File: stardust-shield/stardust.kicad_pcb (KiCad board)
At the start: 2 copper layers, 154.3 x 139.1 mm, 16 parts, among them J1 BEXUS 28V, J2 Pololu J8557, J3 Pololu J9251, J4 DS3231M, U5 DS18B20, U6 DS18B20, U8 DHT22, U9 SSCDRNN015PASA5

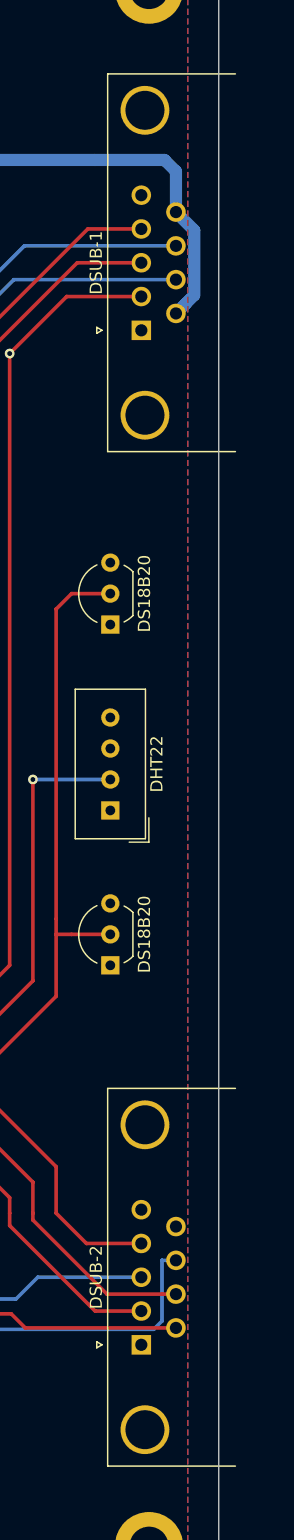
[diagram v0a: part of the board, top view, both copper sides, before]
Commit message: add db9 models, and update footprints
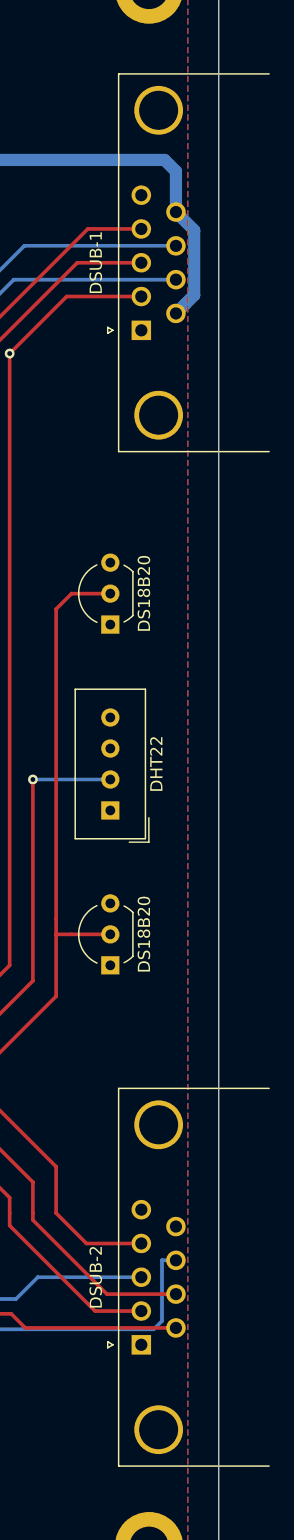
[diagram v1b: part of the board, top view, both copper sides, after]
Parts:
- DSUB-1, DSUB-2: footprint Connector_Dsub:DSUB-9_Male_Horizontal_P2.77x2.84mm_EdgePinOffset4.94mm_Housed_MountingHolesOffset7.48mm -> Connector_Dsub:DSUB-9_Male_Horizontal_P2.77x2.84mm_EdgePinOffset7.70mm_Housed_MountingHolesOffset9.12mm

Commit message: rev.2 init
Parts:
- removed the REF** at (88.9, 151.1)
- removed the REF** at (231.8, 151.1)
- removed the REF** at (88.9, 23.5)
- removed the REF** at (231.8, 23.5)
- added J4: Pololu J9251 Servo, Connector_PinSocket_2.54mm:PinSocket_1x05_P2.54mm_Vertical, F.Cu at (113.7, 76.0)
- added REF**: MountingHole_3.2mm_M3_DIN965_Pad, MountingHole:MountingHole_3.2mm_M3_DIN965_Pad, F.Cu at (165.7, 125.1)
- added REF**: MountingHole_3.2mm_M3_DIN965_Pad, MountingHole:MountingHole_3.2mm_M3_DIN965_Pad, F.Cu at (165.7, 60.2)
- added REF**: MountingHole_3.2mm_M3_DIN965_Pad, MountingHole:MountingHole_3.2mm_M3_DIN965_Pad, F.Cu at (75.0, 60.2)
- added REF**: MountingHole_3.2mm_M3_DIN965_Pad, MountingHole:MountingHole_3.2mm_M3_DIN965_Pad, F.Cu at (74.9, 125.1)
- Arduino Mega 2560: renamed from XA1
- moved J1 110.9 mm to (75.7, 97.7), turned to 90 degrees
- moved J2 95.6 mm to (91.0, 87.1), turned to 0 degrees
- moved U5 72.4 mm to (156.4, 80.0)
- moved U6 72.4 mm to (156.4, 108.0)
- moved U8 72.4 mm to (156.4, 95.3)
- moved Servos 63.4 mm to (175.3, 81.3)
- moved J3 62.2 mm to (113.7, 98.5), turned to 0 degrees
- moved Sensors 59.3 mm to (175.2, 114.9)
- moved U9 57.7 mm to (143.7, 91.0)
- moved R1 49.8 mm to (144.1, 78.7)
- moved Arduino Mega 2560 29.5 mm to (69.2, 118.7)
- moved J5 17.5 mm to (149.5, 71.7), turned to 270 degrees
- renumbered J4 to J5, DSUB-2 to Sensors, DSUB-1 to Servos
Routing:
- net Pump-GPIO: track 109.1 -> 0.00 mm, vias 2 -> 0
- net I2C-SDA: track 107.9 -> 0.00 mm, vias 3 -> 0
- net I2C-SCL: track 106.9 -> 0.00 mm, vias 1 -> 0
- net 1Wire-1: track 104.9 -> 0.00 mm, vias 1 -> 0
- net SPI-CLK: track 104.5 -> 0.00 mm, vias 3 -> 0
- net DHT22-1: track 103.6 -> 0.00 mm, vias 1 -> 0
- net SPI-MISO: track 94.6 -> 0.00 mm, vias 3 -> 0
- net 1Wire-3: track 88.0 -> 0.00 mm
- net +12V: track 74.5 -> 0.00 mm
- net DHT22-3: track 67.2 -> 0.00 mm, vias 1 -> 0
- net SPI-SS-Pressure-1: track 61.7 -> 0.00 mm
- net 1Wire-2: track 58.6 -> 0.00 mm
- net DHT22-2: track 57.9 -> 0.00 mm
- net +28V: track 55.0 -> 0.00 mm
- net SPI-MOSI: track 54.8 -> 0.00 mm
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- removed copper zone on F.Cu, net +5V
- removed copper zone on B.Cu, net GND
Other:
- board size 154.3 x 139.1 mm -> 113 x 76.3 mm

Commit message: 2.0
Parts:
- removed the REF** at (165.7, 125.1)
- removed the REF** at (165.7, 60.2)
- removed the REF** at (75.0, 60.2)
- removed the REF** at (74.9, 125.1)
- added J5: Pololu J9251 Servo, Connector_PinSocket_2.54mm:PinSocket_1x05_P2.54mm_Vertical, F.Cu at (90.8, 151.1)
- added J7: VMA430, Connector_PinHeader_2.54mm:PinHeader_1x05_P2.54mm_Vertical, F.Cu at (76.3, 97.2)
- added R2: 4.7k, Resistor_SMD:R_0603_1608Metric, F.Cu at (175.3, 111.3)
- added R3: 4.7k, Resistor_SMD:R_0603_1608Metric, F.Cu at (174.7, 107.8)
- added R4: 4.7k, Resistor_SMD:R_0603_1608Metric, F.Cu at (153.2, 83.2)
- added R5: 200m, Resistor_SMD:R_0603_1608Metric, F.Cu at (69.8, 144.1)
- added R6: 200m, Resistor_SMD:R_0603_1608Metric, F.Cu at (90.8, 144.1)
- added R7: 200m, Resistor_SMD:R_0603_1608Metric, F.Cu at (111.8, 144.1)
- added R9: 200m, Resistor_SMD:R_0603_1608Metric, F.Cu at (133.3, 144.3)
- added REF**: MountingHole_3.2mm_M3_DIN965_Pad, MountingHole:MountingHole_3.2mm_M3_DIN965_Pad, F.Cu at (153.0, 148.6)
- added REF**: MountingHole_3.2mm_M3_DIN965_Pad, MountingHole:MountingHole_3.2mm_M3_DIN965_Pad, F.Cu at (153.0, 75.6)
- added REF**: MountingHole_3.2mm_M3_DIN965_Pad, MountingHole:MountingHole_3.2mm_M3_DIN965_Pad, F.Cu at (52.1, 148.6)
- added REF**: MountingHole_3.2mm_M3_DIN965_Pad, MountingHole:MountingHole_3.2mm_M3_DIN965_Pad, F.Cu at (52.1, 75.6)
- added U1: INA181, Package_TO_SOT_SMD:SOT-23-6, F.Cu at (64.8, 144.1)
- added U2: INA181, Package_TO_SOT_SMD:SOT-23-6, F.Cu at (85.7, 144.1)
- added U3: INA181, Package_TO_SOT_SMD:SOT-23-6, F.Cu at (106.7, 144.1)
- added U4: INA181, Package_TO_SOT_SMD:SOT-23-6, F.Cu at (128.3, 144.1)
- J3: value Pololu J9251 -> Pololu J8557
- J4: value Pololu J9251 Servo -> Pololu J9251
- J6: renamed from J5; footprint Connector_PinHeader_2.54mm:PinHeader_1x05_P2.54mm_Vertical -> Socket:RTC-DS3231M
- R1: moved to F.Cu
- XA1: renamed from Arduino Mega 2560
- moved J4 87.0 mm to (69.8, 151.1), turned to 270 degrees
- moved J2 67.3 mm to (111.8, 151.1), turned to 270 degrees
- moved DSUB-Servo1 57.7 mm to (151.8, 134.0)
- moved J3 56.1 mm to (133.3, 151.1), turned to 270 degrees
- moved J6 54.7 mm to (99.6, 94.1)
- moved J1 47.2 mm to (50.8, 137.8), turned to 270 degrees
- moved U5 40.6 mm to (118.3, 94.0)
- moved U6 40.6 mm to (118.3, 121.9)
- moved U8 40.6 mm to (118.3, 109.2)
- moved R1 35.7 mm to (174.1, 98.2), turned to 270 degrees
- moved DSUB-Sensor1 27.3 mm to (151.8, 101.0)
- moved XA1 27.1 mm to (46.4, 133.3)
- moved U9 20.2 mm to (129.5, 105.4), turned to 270 degrees
- renumbered Sensors to DSUB-Sensor1, Servos to DSUB-Servo1
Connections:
- net Net-(XA1-PadD16) renamed TX2
- net Net-(XA1-PadD17) renamed RX2
- net Net-(XA1-PadD18) renamed TX1
- net Net-(XA1-PadD19) renamed RX1
- DSUB-Servo1 pad 5: +5V -> +5P
- DSUB-Servo1 pad 9: +12V -> +12P
- J1 pad 1: +28V -> GND
- J1 pad 2: GND -> +28V
- J2 pad 1: +12V -> Net-(J2-Pad1)
- J3 pad 1: +5V -> Net-(J3-Pad1)
- J4 pad 1: +5V -> Net-(J4-Pad1)
- XA1 pad A1: Net-(XA1-PadA1) -> INA1
- XA1 pad A2: Net-(XA1-PadA2) -> INA2
- XA1 pad A3: Net-(XA1-PadA3) -> INA3
- XA1 pad A4: Net-(XA1-PadA4) -> INA4
- XA1 pad D14: Net-(XA1-PadD14) -> TX3
- XA1 pad D15: Net-(XA1-PadD15) -> RX3
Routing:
- net +28V: track 0.00 -> 92.5 mm
- net +5P: track 0.00 -> 85.0 mm, vias 0 -> 4
- net +5V: track 0.00 -> 67.1 mm, vias 0 -> 4
- net +12V: track 0.00 -> 56.3 mm, vias 0 -> 4
- net INA1: track 0.00 -> 51.6 mm
- net 1Wire-3: track 0.00 -> 50.2 mm
- net +12P: track 0.00 -> 45.6 mm, vias 0 -> 4
- net SPI-CLK: track 0.00 -> 38.5 mm
- net SPI-MISO: track 0.00 -> 34.8 mm
- net Net-(XA1-PadD53): track 0.00 -> 34.0 mm
- net INA2: track 0.00 -> 33.8 mm
- net INA4: track 0.00 -> 31.8 mm
- net INA3: track 0.00 -> 16.5 mm
- net GND: track 0.00 -> 11.5 mm, vias 0 -> 5
- net Net-(J5-Pad1): track 0.00 -> 10.5 mm
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- added copper zone on F.Cu, net +5V
- added copper zone on B.Cu, net GND
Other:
- board size 113 x 76.3 mm -> 112.4 x 84.5 mm

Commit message: final 2.0
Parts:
- removed the R1 at (174.1, 98.2)
- removed the REF** at (153.0, 148.6)
- removed the REF** at (52.1, 148.6)
- added C1: 1mF, Capacitor_SMD:C_0603_1608Metric_Pad1.05x0.95mm_HandSolder, F.Cu at (65.9, 137.8)
- added C2: 1mF, Capacitor_SMD:C_0603_1608Metric_Pad1.05x0.95mm_HandSolder, F.Cu at (87.0, 137.8)
- added C3: 1mF, Capacitor_SMD:C_0603_1608Metric_Pad1.05x0.95mm_HandSolder, F.Cu at (108.2, 137.8)
- added C4: 1mF, Capacitor_SMD:C_0603_1608Metric_Pad1.05x0.95mm_HandSolder, F.Cu at (130.0, 137.8)
- added D1: LED, LED_SMD:LED_0603_1608Metric_Pad1.05x0.95mm_HandSolder, F.Cu at (104.8, 79.2)
- added D2: LED, LED_SMD:LED_0603_1608Metric_Pad1.05x0.95mm_HandSolder, F.Cu at (102.2, 79.2)
- added D3: LED, LED_SMD:LED_0603_1608Metric_Pad1.05x0.95mm_HandSolder, F.Cu at (99.7, 79.2)
- added D4: LED, LED_SMD:LED_0603_1608Metric_Pad1.05x0.95mm_HandSolder, F.Cu at (97.2, 79.2)
- added D5: LED, LED_SMD:LED_0603_1608Metric_Pad1.05x0.95mm_HandSolder, F.Cu at (94.6, 79.2)
- added D6: LED, LED_SMD:LED_0603_1608Metric_Pad1.05x0.95mm_HandSolder, F.Cu at (92.1, 79.3)
- added J7'1: VMA430, Connector_PinHeader_2.54mm:PinHeader_1x05_P2.54mm_Vertical, F.Cu at (76.7, 97.0)
- added R12: 10k, Resistor_SMD:R_0603_1608Metric_Pad1.05x0.95mm_HandSolder, B.Cu at (137.2, 97.0)
- added R13: 10k, Resistor_SMD:R_0603_1608Metric_Pad1.05x0.95mm_HandSolder, B.Cu at (137.2, 108.8)
- added R14: 1k, Resistor_SMD:R_0603_1608Metric_Pad1.05x0.95mm_HandSolder, F.Cu at (104.8, 75.1)
- added R15: 1k, Resistor_SMD:R_0603_1608Metric_Pad1.05x0.95mm_HandSolder, F.Cu at (102.2, 75.1)
- added R16: 1k, Resistor_SMD:R_0603_1608Metric_Pad1.05x0.95mm_HandSolder, F.Cu at (99.7, 75.1)
- added R17: 1k, Resistor_SMD:R_0603_1608Metric_Pad1.05x0.95mm_HandSolder, F.Cu at (97.2, 75.1)
- added R18: 1k, Resistor_SMD:R_0603_1608Metric_Pad1.05x0.95mm_HandSolder, F.Cu at (94.6, 75.1)
- added R19: 1k, Resistor_SMD:R_0603_1608Metric_Pad1.05x0.95mm_HandSolder, F.Cu at (92.1, 75.1)
- added R2: 16k, Resistor_SMD:R_0603_1608Metric, F.Cu at (61.5, 138.7)
- added R4: 16k, Resistor_SMD:R_0603_1608Metric_Pad1.05x0.95mm_HandSolder, F.Cu at (82.5, 138.7)
- added R6: 16k, Resistor_SMD:R_0603_1608Metric_Pad1.05x0.95mm_HandSolder, F.Cu at (103.6, 138.7)
- added R8: 16k, Resistor_SMD:R_0603_1608Metric_Pad1.05x0.95mm_HandSolder, F.Cu at (125.0, 138.7)
- added REF**: TestPoint_Pad_D1.0mm, TestPoint:TestPoint_Pad_D1.0mm, F.Cu at (73.4, 139.2)
- added REF**: TestPoint_Pad_D1.0mm, TestPoint:TestPoint_Pad_D1.0mm, F.Cu at (134.1, 142.0)
- added REF**: TestPoint_Pad_D1.0mm, TestPoint:TestPoint_Pad_D1.0mm, F.Cu at (113.0, 141.5)
- added REF**: TestPoint_Pad_D1.0mm, TestPoint:TestPoint_Pad_D1.0mm, F.Cu at (93.0, 140.7)
- added REF**: MountingHole_3.2mm_M3_DIN965_Pad, MountingHole:MountingHole_3.2mm_M3_DIN965_Pad, F.Cu at (153.0, 149.6)
- added REF**: MountingHole_3.2mm_M3_DIN965_Pad, MountingHole:MountingHole_3.2mm_M3_DIN965_Pad, F.Cu at (52.1, 149.6)
- added SW1: SW_Push, Button_Switch_THT:SW_TH_Tactile_Omron_B3F-10xx, F.Cu at (128.5, 99.6)
- added SW2: SW_Push, Button_Switch_THT:SW_TH_Tactile_Omron_B3F-10xx, F.Cu at (128.5, 106.7)
- R11: renamed from R4; moved to B.Cu
- moved R9 34.1 mm to (148.2, 132.0), turned to 90 degrees
- moved R10 31.9 mm to (147.2, 91.7), turned to 270 degrees
- moved U6 29.0 mm to (126.4, 94.1)
- moved R11 17.7 mm to (137.2, 90.7), turned to 270 degrees
- moved U9 14.5 mm to (128.3, 119.9)
- moved U5 14.4 mm to (132.6, 94.1)
- moved J7 9.27 mm to (85.6, 97.2)
- moved U8 4.95 mm to (121.4, 105.4)
- turned J6 to 0 degrees
- renumbered R5 to R1, R3 to R10, R6 to R3, R7 to R5, R9 to R7, R2 to R9
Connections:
- DSUB-Servo1 pad 3: Pump-GPIO -> Net-(DSUB-Servo1-Pad3)
- J2 pad 4: Net-(J2-Pad4) -> DC-Pump-1
- J3 pad 4: Net-(J3-Pad4) -> DC-Pump-2
- J5 pad 4: Net-(J5-Pad4) -> DC-Servo
- U1 pad 1: INA1 -> Net-(R2-Pad1)
- U2 pad 1: INA2 -> Net-(R4-Pad1)
- U3 pad 1: INA3 -> Net-(R6-Pad1)
- U4 pad 1: INA4 -> Net-(R8-Pad1)
- XA1 pad A2: INA2 -> DC-Servo
- XA1 pad A3: INA3 -> INA2
- XA1 pad A4: INA4 -> DC-Pump-1
- XA1 pad A5: Net-(XA1-PadA5) -> INA3
- XA1 pad A6: Net-(XA1-PadA6) -> DC-Pump-2
- XA1 pad A7: Net-(XA1-PadA7) -> INA4
- XA1 pad D2: Net-(XA1-PadD2) -> LED-1
- XA1 pad D25: SPI-SS-Pressure-2 -> Net-(XA1-PadD25)
- XA1 pad D27: DHT22-1 -> Net-(XA1-PadD27)
- XA1 pad D28: Net-(XA1-PadD28) -> 1Wire-3
- XA1 pad D29: Pump-GPIO -> 1Wire-2
- XA1 pad D3: Net-(XA1-PadD3) -> LED-2
- XA1 pad D31: 1Wire-1 -> Net-(XA1-PadD31)
- XA1 pad D32: Net-(XA1-PadD32) -> Button-1
- XA1 pad D33: DHT22-3 -> SPI-SS-Pressure-1
- XA1 pad D35: 1Wire-3 -> DHT22-2
- XA1 pad D36: Net-(XA1-PadD36) -> DHT22-3
- XA1 pad D37: 1Wire-2 -> Net-(XA1-PadD37)
- XA1 pad D39: SPI-SS-Pressure-1 -> Net-(XA1-PadD39)
- XA1 pad D4: Net-(XA1-PadD4) -> LED-3
- XA1 pad D40: Net-(XA1-PadD40) -> Button-2
- XA1 pad D41: DHT22-2 -> Net-(XA1-PadD41)
- XA1 pad D45: Net-(XA1-PadD45) -> DHT22-1
- XA1 pad D47: Net-(XA1-PadD47) -> 1Wire-1
- XA1 pad D48: Net-(XA1-PadD48) -> SPI-SS-Pressure-2
- XA1 pad D5: Net-(XA1-PadD5) -> LED-4
- XA1 pad D6: Net-(XA1-PadD6) -> LED-5
- XA1 pad D7: Net-(XA1-PadD7) -> LED-6
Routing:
- net I2C-SDA: track 0.00 -> 118.7 mm, vias 0 -> 1
- net I2C-SCL: track 0.00 -> 114.7 mm, vias 0 -> 1
- net RX3: track 0.00 -> 56.6 mm
- net TX3: track 0.00 -> 52.8 mm
- net GND: track 11.5 -> 54.2 mm, vias 5 -> 17
- net DC-Servo: track 0.00 -> 40.2 mm
- net SPI-MOSI: track 0.38 -> 39.7 mm
- net 1Wire-3: track 50.2 -> 14.5 mm
- net Net-(XA1-PadD53): track 34.0 -> 0.00 mm
- net DC-Pump-2: track 0.00 -> 28.9 mm
- net +5V: track 67.1 -> 95.5 mm, vias 4 -> 16
- net SPI-CLK: track 38.5 -> 64.1 mm
- net DC-Pump-1: track 0.00 -> 23.6 mm
- net 1Wire-1: track 0.00 -> 23.2 mm, vias 0 -> 2
- net SPI-SS-Pressure-2: track 0.00 -> 19.9 mm, vias 0 -> 1
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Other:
- board size 112.4 x 84.5 mm -> 112.4 x 85.5 mm

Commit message: tweaks
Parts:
- added D7: D_TVS, Diode_SMD:D_SOD-323_HandSoldering, B.Cu at (54.4, 140.5)
- moved SW1 3.12 mm to (128.5, 96.5)
- moved U5 1.06 mm to (131.6, 94.1)
- moved U6 0.89 mm to (125.5, 94.1)
- moved R12 0.63 mm to (137.7, 96.7)
- moved R13 0.56 mm to (137.7, 109.1)
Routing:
- net +5V: track 95.5 -> 101.3 mm
- net +28V: track 93.1 -> 95.1 mm
- net 1Wire-3: track 14.5 -> 15.3 mm

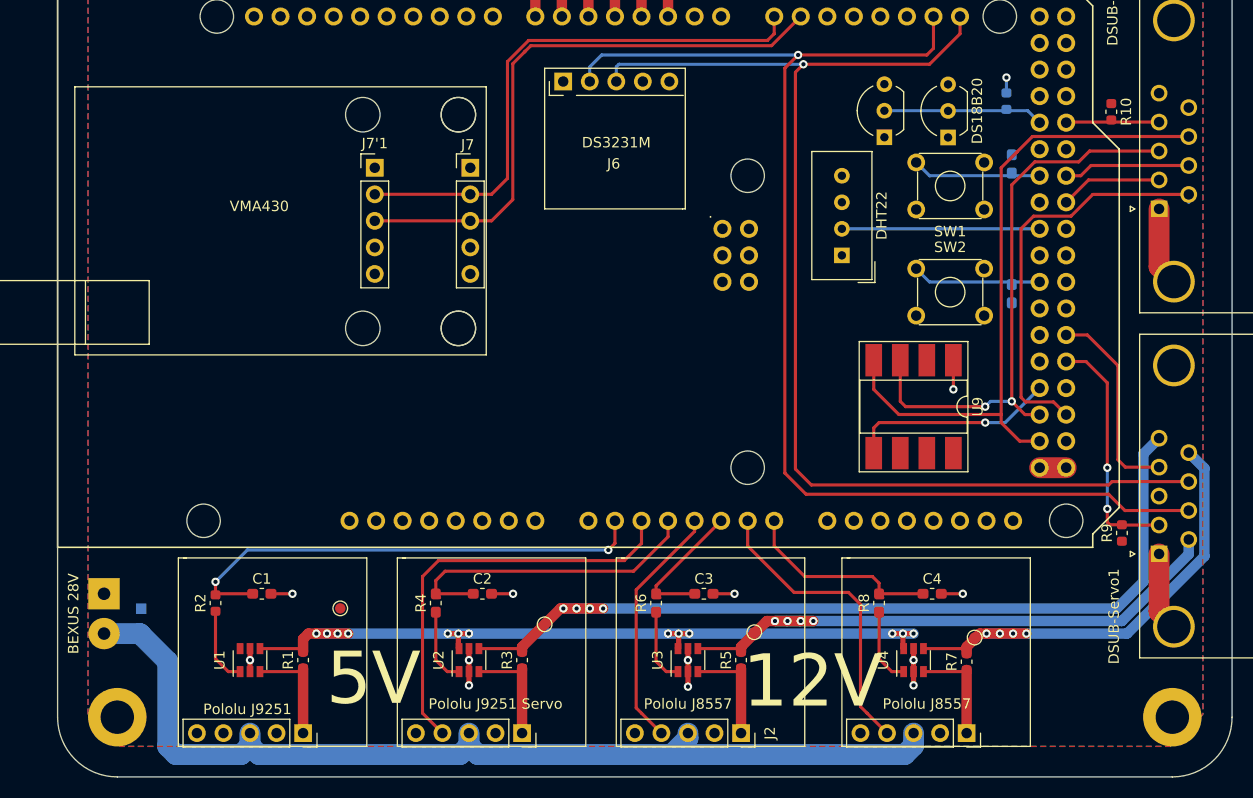
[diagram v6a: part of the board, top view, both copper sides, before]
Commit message: add capacitors
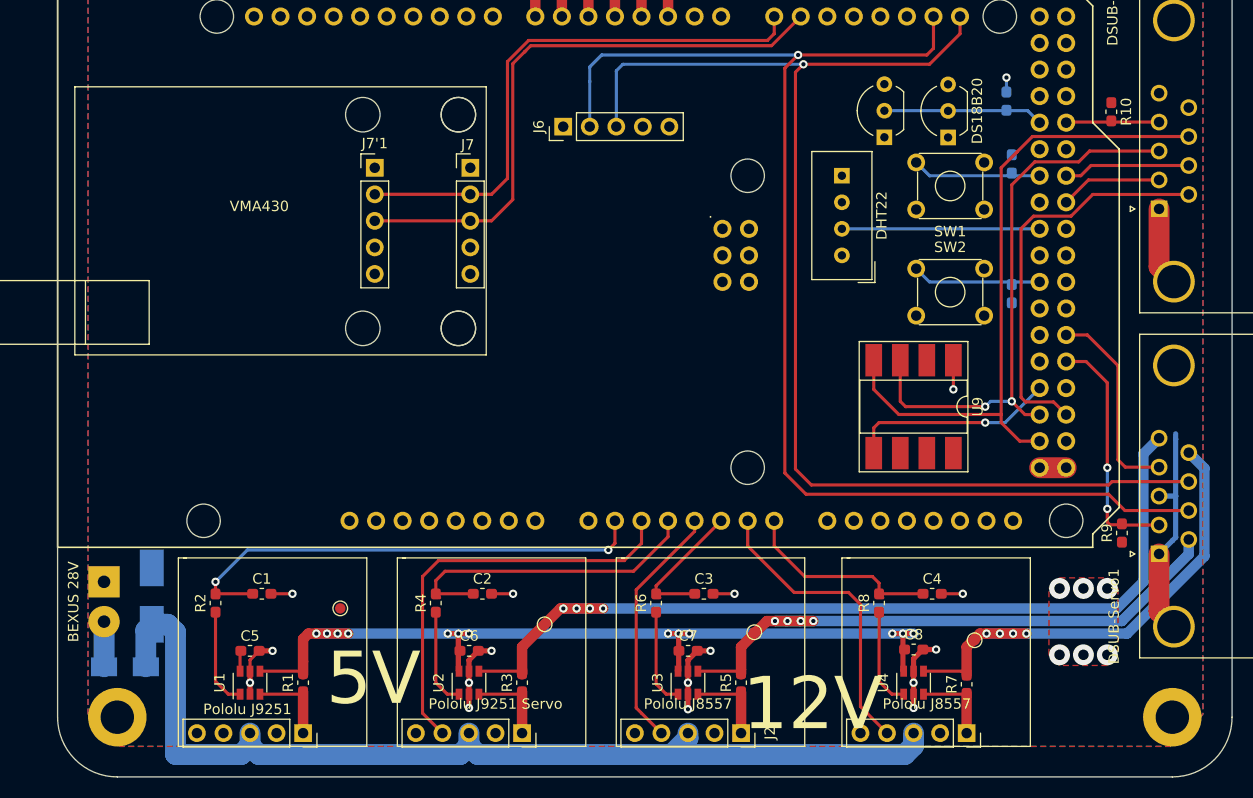
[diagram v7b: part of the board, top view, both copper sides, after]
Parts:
- added C5: 100uF, Capacitor_SMD:C_0603_1608Metric_Pad1.05x0.95mm_HandSolder, F.Cu at (64.8, 143.3)
- added C6: 100uF, Capacitor_SMD:C_0603_1608Metric_Pad1.05x0.95mm_HandSolder, F.Cu at (85.7, 143.3)
- added C7: 100uF, Capacitor_SMD:C_0603_1608Metric_Pad1.05x0.95mm_HandSolder, F.Cu at (106.7, 143.3)
- added C8: 100uF, Capacitor_SMD:C_0603_1608Metric_Pad1.05x0.95mm_HandSolder, F.Cu at (128.3, 143.1)
- added D8: D_Schottky, Diode_SMD:D_SMA, B.Cu at (52.8, 144.8)
- C1, C2, C3, C4: value 1mF -> 1uF
- D7: footprint Diode_SMD:D_SOD-323_HandSoldering -> Diode_SMD:D_SMB_Handsoldering
- J6: footprint Socket:RTC-DS3231M -> Connector_PinHeader_2.54mm:PinHeader_1x05_P2.54mm_Vertical
- R1, R10, R11, R2, R3, R5, R7, R9: footprint Resistor_SMD:R_0603_1608Metric -> Resistor_SMD:R_0603_1608Metric_Pad1.05x0.95mm_HandSolder
- moved J6 4.93 mm to (94.7, 93.1), turned to 90 degrees
- moved D7 2.67 mm to (55.4, 138.0)
- moved R1 2.16 mm to (69.8, 146.3)
- moved R3 2.16 mm to (90.8, 146.3)
- moved R5 2.16 mm to (111.8, 146.3)
- moved R7 2.16 mm to (133.3, 146.5)
- moved U1 2.16 mm to (64.8, 146.3)
- moved U2 2.16 mm to (85.7, 146.3)
- moved U3 2.16 mm to (106.7, 146.3)
- moved U4 2.16 mm to (128.3, 146.3)
- moved J1 1.14 mm to (50.8, 136.7)
- moved REF** 0.25 mm to (134.1, 142.2)
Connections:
- DSUB-Sensor1 pad 9: Net-(DSUB-Sensor1-Pad9) -> GND
- DSUB-Servo1 pad 3: Net-(DSUB-Servo1-Pad3) -> GND
- J1 pad 2: +28V -> Net-(D8-Pad2)
- REF** pad 1: (no net) -> +12P
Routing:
- net GND: track 54.2 -> 82.7 mm, vias 17 -> 27
- net +5V: track 101.3 -> 112.3 mm
- net Net-(D8-Pad2): track 0.00 -> 4.32 mm
- net I2C-SDA: track 118.7 -> 123.1 mm
- net I2C-SCL: track 114.7 -> 118.8 mm
- net +5P: track 88.8 -> 91.3 mm
- net Net-(J5-Pad1): track 10.5 -> 8.21 mm
- net Net-(J4-Pad1): track 10.5 -> 8.21 mm
- net Net-(J3-Pad1): track 10.2 -> 7.99 mm
- net Net-(J2-Pad1): track 10.5 -> 8.21 mm
- net +28V: track 95.1 -> 97.3 mm
- net +12V: track 60.0 -> 62.2 mm
- net Net-(R6-Pad1): track 7.21 -> 9.37 mm
- net Net-(R8-Pad1): track 7.32 -> 9.48 mm
- net Net-(R4-Pad1): track 7.27 -> 9.43 mm
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- added copper zone on F.Cu, net GND

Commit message: final touches
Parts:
- removed the REF** at (134.1, 142.2)
- removed the REF** at (113.0, 141.5)
- removed the REF** at (93.0, 140.7)
- added REF**: TestPoint_Pad_D1.0mm, TestPoint:TestPoint_Pad_D1.0mm, B.Cu at (146.8, 141.6)
- added REF**: TestPoint_Pad_D1.0mm, TestPoint:TestPoint_Pad_D1.0mm, B.Cu at (144.5, 140.5)
- added REF**: TestPoint_Pad_D1.0mm, TestPoint:TestPoint_Pad_D1.0mm, B.Cu at (142.2, 139.2)
- moved J6 9.14 mm to (94.7, 102.2)
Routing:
- net I2C-SDA: track 123.1 -> 125.4 mm, vias 1 -> 3
- net I2C-SCL: track 118.8 -> 120.1 mm, vias 1 -> 3
